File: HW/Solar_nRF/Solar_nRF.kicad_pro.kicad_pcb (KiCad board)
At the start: 2 copper layers, 60 x 80 mm, 87 parts, among them J1 Conn_01x02, J10 Conn_01x02, J11 Conn_01x02, J13 Conn_02x03_Odd_Even, J2 Conn_01x04, J3 Conn_01x02, J4 Conn_01x02, J5 Conn_01x02, J6 Conn_01x04, J7 Conn_01x04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

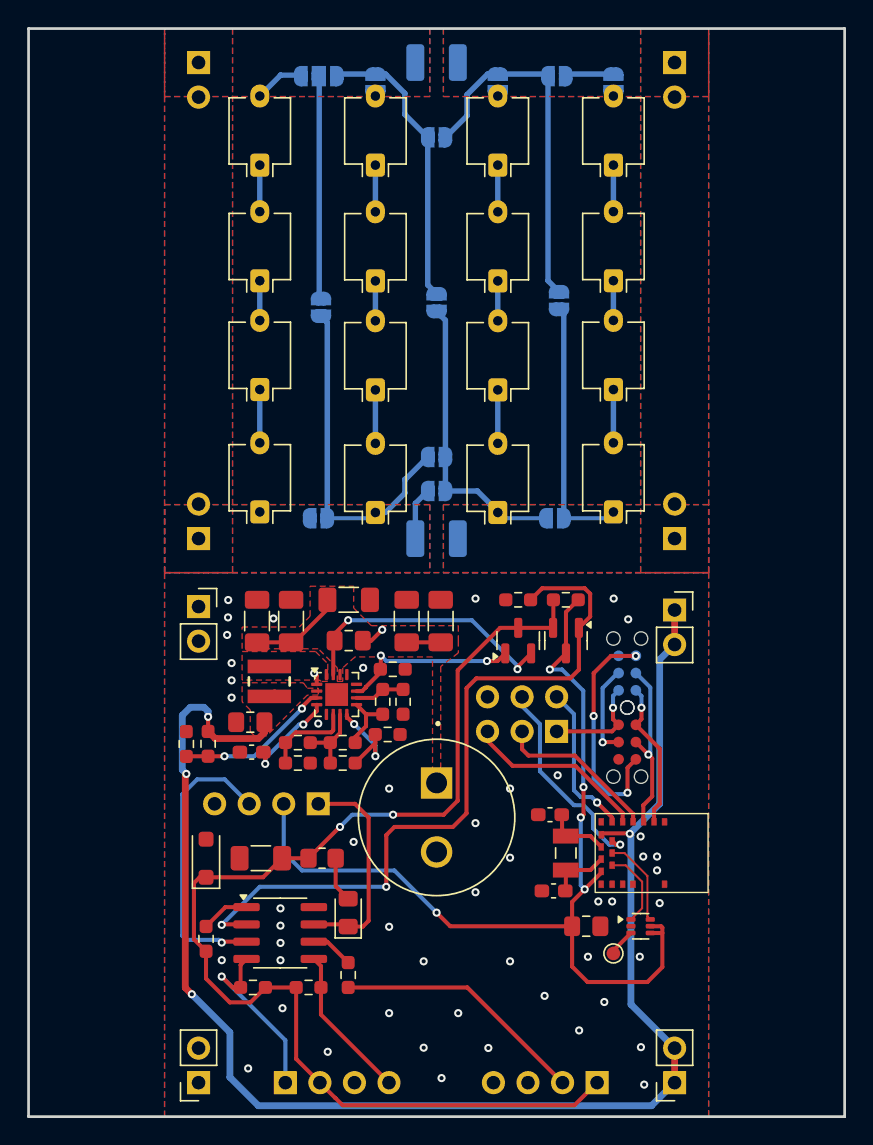
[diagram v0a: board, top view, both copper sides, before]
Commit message: Updated SCH & PCB based with fixes found during development
Inverted bat_ok signal
Cleaned up layout, removing solar array and replacing with a single photodiode
Connected nRF to +V programming pad
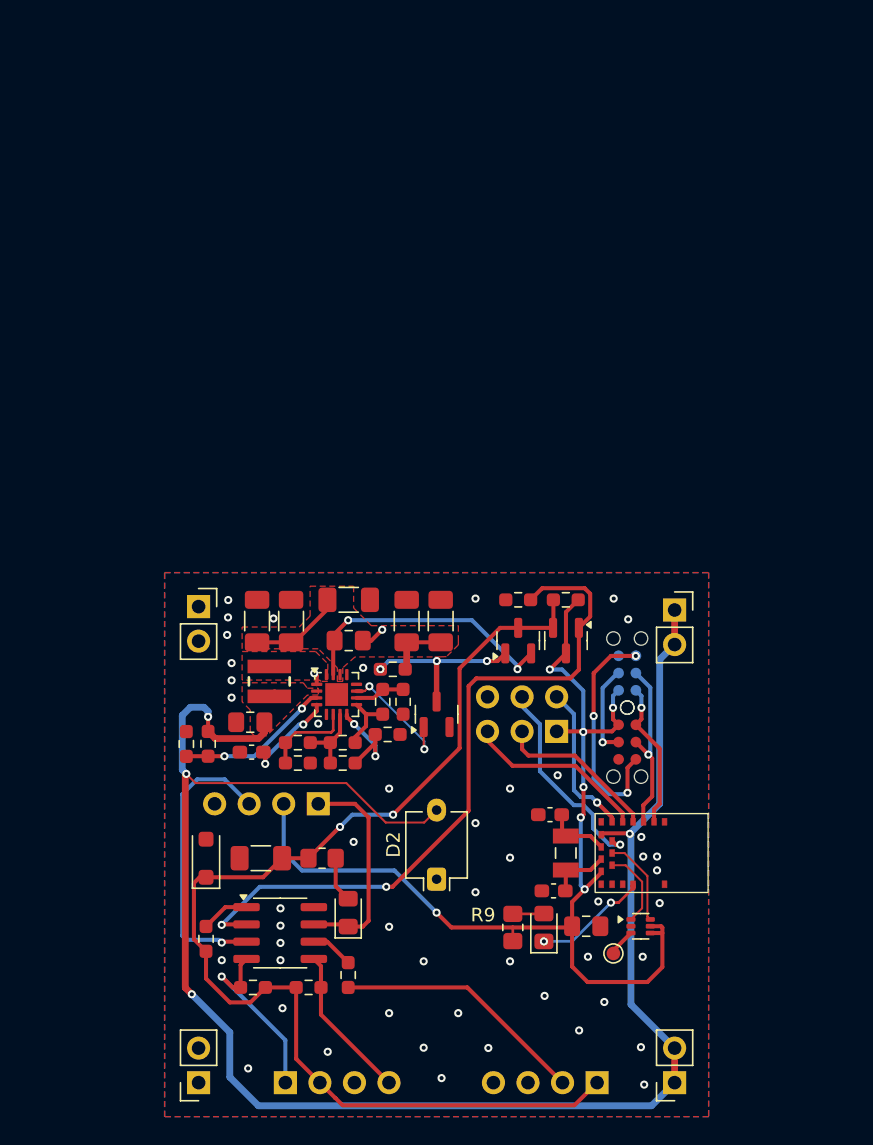
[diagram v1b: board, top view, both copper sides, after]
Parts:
- removed C10, C11: 100u, Capacitor_SMD:C_1210_3225Metric_Pad1.33x2.70mm_HandSolder
- removed D21, D22, D23, D24, D25, D26, D27, D28, D29, D30, D31, D32, D33, D34, D35, D36: BPW34, OptoDevice:Osram_DIL2_4.3x4.65mm_P5.08mm
- removed J1, J3, J8, J9: Conn_01x02, Connector_PinSocket_2.54mm:PinSocket_1x02_P2.54mm_Vertical
- removed JP15, JP16, JP17, JP18, JP19, JP20, JP21, JP22, JP23, JP24, JP25, JP26, JP27, JP28: SolderJumper_2_Open, Jumper:SolderJumper-2_P1.3mm_Open_RoundedPad1.0x1.5mm
- removed SC1: 100mF, FT0H104ZF:CAPPRD508W154D1200H850
- added D2: BPW34, OptoDevice:Osram_DIL2_4.3x4.65mm_P5.08mm, F.Cu at (60.5, 86.0)
- added D3: LED, LED_SMD:LED_0805_2012Metric_Pad1.15x1.40mm_HandSolder, F.Cu at (68.4, 89.6)
- added Q3: IRLML6244, Package_TO_SOT_SMD:SOT-23, F.Cu at (60.5, 73.9)
- added R9: R, Resistor_SMD:R_0805_2012Metric_Pad1.20x1.40mm_HandSolder, F.Cu at (66.1, 89.6)
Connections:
- J13 pad 1: /Sensors and Processing/VDD -> VCC_SW_P
- R7 pad 2: GND -> Net-(U1-VBAT)
- TC1 pad 1: /Sensors and Processing/VDD -> VCC_SW_P
- TC2 pad 1: /Sensors and Processing/VDD -> VCC_SW_P
- U1 pad 11: Net-(Q1-G) -> Net-(Q3-G)
- U3 pad 18: unconnected-(U3-P0.20-Pad18) -> /Sensors and Processing/LED_ENN
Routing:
- net Net-(JP22-A): track 26.6 -> 0.00 mm
- net Net-(D28-K): track 24.9 -> 0.00 mm
- net Net-(D32-K): track 22.6 -> 0.00 mm
- net Net-(JP18-A): track 21.4 -> 0.00 mm
- net Net-(D36-K): track 19.3 -> 0.00 mm
- net +PD: track 115.3 -> 132.0 mm
- net Net-(JP15-B): track 16.4 -> 0.00 mm
- net Net-(Q3-G): track 0.00 -> 9.61 mm, vias 0 -> 2
- net VCC_SW_P: track 71.1 -> 79.8 mm, vias 5 -> 7
- net /Sensors and Processing/LED_ENN: track 0.00 -> 8.46 mm, vias 0 -> 2
- net /Sensors and Processing/VDD: track 7.63 -> 0.00 mm, vias 1 -> 0
- net Net-(D21-A): track 4.21 -> 0.00 mm
- net Net-(D31-K): track 3.93 -> 0.00 mm
- net Net-(D27-K): track 3.93 -> 0.00 mm
- net Net-(D35-K): track 3.92 -> 0.00 mm
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- removed copper zone on B.Cu, net +PD
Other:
- board outline removed
